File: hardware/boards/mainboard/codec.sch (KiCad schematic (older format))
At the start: 22 parts, among them U1 CS42448

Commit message: mainboard
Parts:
- removed C11, C12, C13, C14: 4.7uf, Mainboard:AVX-A, symbol Mainboard-eagle-import:TANTALUM-SMD-4.7UF-16V(AVX-A)
- added C11, C12, C13, C14: 4.7uF, Capacitors_Tantalum_SMD:CP_Tantalum_Case-A_EIA-3216-18_Reflow, symbol Device:CP
- R1, R2, R3: footprint Mainboard:R0805 -> Resistors_SMD:R_0805
- R4: footprint Mainboard:R0805 -> Oddities:NetTie-I_Connected_SMD; symbol Mainboard-eagle-import:ZERO-OHM-LINK -> Device:Net-Tie_2
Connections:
- net 3V3: no longer C15.2, R2.1, R3.1, U1.3 (~RST~)
- net AGND: now also C11.2, C12.2, C13.2, C14.2
- net GND: no longer C15.1, R4.1, U1.2 (AD1/CDIN), U1.23 (DGND@23), U1.62 (DGND@62), U1.7 (DGND@7)
- net at U1.45 (AIN1-): now also C11.1
- net at U1.47 (AIN2-): now also C12.1
- net at U1.49 (AIN3-): now also C13.1
- net at U1.51 (AIN4-): now also C14.1
- new net: R4.1, U1.23 (DGND@23), U1.62 (DGND@62), U1.7 (DGND@7)
- new net +3V3: C15.2, R2.1, R3.1, U1.3 (~RST~)
- no-connect marks 0 -> 16
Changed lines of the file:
@@
 $Descr User 13529 9224
 encoding utf-8
-Sheet 5 13
+Sheet 5 12
 Title ""
 Date ""
@@
 Wire Wire Line
 	4600 6500 4900 6500
-Text GLabel 4600 6700 0    10   BiDi ~ 0
-GND
 Wire Wire Line
 	4900 5400 4900 5500
@@
 Wire Wire Line
 	6300 7300 6300 8350
-Wire Wire Line
-	6300 8350 6650 8350
 Connection ~ 6100 7300
 Connection ~ 6200 7300
 Connection ~ 6300 7300
-Text GLabel 6100 7300 0    10   BiDi ~ 0
-GND
 Wire Wire Line
 	4150 650  4150 450
-Text GLabel 4150 650  0    10   BiDi ~ 0
-GND
 Wire Wire Line
 	7100 2100 7100 2200
@@
 	4300 7000 4900 7000
 Connection ~ 4100 7000
-Text GLabel 4200 7000 2    70   BiDi ~ 0
-3V3
 Connection ~ 4300 7000
 Wire Wire Line
 	3550 150  4150 150
-Wire Wire Line
-	4150 150  4750 150
-Connection ~ 4150 150
 Text GLabel 3550 150  0    70   BiDi ~ 0
-3V3
++3V3
 Wire Wire Line
 	1150 2500 4900 2500
@@
 	4900 2700 4800 2700
 Wire Wire Line
-	3050 2000 4600 2000
-Wire Wire Line
-	4600 2000 4600 3300
+	4600 2150 4600 3300
 Wire Wire Line
 	4600 3300 4900 3300
@@
 Wire Wire Line
 	4650 3900 4900 3900
-Wire Wire Line
-	9750 1850 10200 1850
-Text Label 10200 1850 0    70   ~ 0
+Text Label 12200 1100 0    70   ~ 0
 AGND
 Wire Wire Line
@@
 Wire Wire Line
 	7350 8350 7350 7500
-Wire Wire Line
-	6950 8350 7350 8350
 Connection ~ 6700 7300
 Connection ~ 9100 7500
@@
 $EndComp
 $Comp
-L Mainboard-eagle-import:3.3V #SUPPLY?
-U 1 1 9BB82FD5
-P 3200 6900
-AR Path="/9BB82FD5" Ref="#SUPPLY?"  Part="1"
-AR Path="/5D773153/9BB82FD5" Ref="#SUPPLY01"  Part="1"
-F 0 "#SUPPLY01" H 3200 6900 50  0001 C CNN
-F 1 "3.3V" H 3200 7010 59  0000 C BNN
-F 2 "" H 3200 6900 50  0001 C CNN
-F 3 "" H 3200 6900 50  0001 C CNN
-	1    3200 6900
-	1    0    0    -1
-$EndComp
-$Comp
 L Mainboard-eagle-import:GND #GND?
 U 1 1 78C00C8D
@@
 AR Path="/5D773153/1D06DB6F" Ref="R2"  Part="1"
 F 0 "R2" H 3950 6800 59  0000 L BNN
-F 1 "2K" H 3950 6620 59  0001 L BNN
-F 2 "Mainboard:R0805" H 4100 6750 50  0001 C CNN
+F 1 "2K" H 3950 6620 59  0000 L BNN
+F 2 "Resistors_SMD:R_0805" H 4100 6750 50  0001 C CNN
 F 3 "" H 4100 6750 50  0001 C CNN
 	1    4100 6750
@@
 AR Path="/5D773153/21D49CC9" Ref="R3"  Part="1"
 F 0 "R3" H 4150 6650 59  0000 L BNN
-F 1 "2K" H 4150 6470 59  0001 L BNN
-F 2 "Mainboard:R0805" H 4300 6600 50  0001 C CNN
+F 1 "2K" H 4150 6470 59  0000 L BNN
+F 2 "Resistors_SMD:R_0805" H 4300 6600 50  0001 C CNN
 F 3 "" H 4300 6600 50  0001 C CNN
 	1    4300 6600
@@
 $EndComp
 $Comp
-L Mainboard-eagle-import:TANTALUM-SMD-4.7UF-16V(AVX-A) C?
-U 1 1 193FF8E5
-P 1150 2650
-AR Path="/193FF8E5" Ref="C?"  Part="1"
-AR Path="/5D773153/193FF8E5" Ref="C11"  Part="1"
-F 0 "C11" H 900 2800 42  0000 L BNN
-F 1 "4.7uf" H 1200 2800 42  0000 L BNN
-F 2 "Mainboard:AVX-A" H 1150 2650 50  0001 C CNN
-F 3 "" H 1150 2650 50  0001 C CNN
-	1    1150 2650
-	0    1    1    0
-$EndComp
-$Comp
-L Mainboard-eagle-import:TANTALUM-SMD-4.7UF-16V(AVX-A) C?
-U 1 1 0925562E
-P 1500 2950
-AR Path="/0925562E" Ref="C?"  Part="1"
-AR Path="/5D773153/0925562E" Ref="C12"  Part="1"
-F 0 "C12" H 1250 3100 42  0000 L BNN
-F 1 "4.7uf" H 1550 3100 42  0000 L BNN
-F 2 "Mainboard:AVX-A" H 1500 2950 50  0001 C CNN
-F 3 "" H 1500 2950 50  0001 C CNN
-	1    1500 2950
-	0    1    1    0
-$EndComp
-$Comp
-L Mainboard-eagle-import:TANTALUM-SMD-4.7UF-16V(AVX-A) C?
-U 1 1 EF1AB486
-P 2250 3550
-AR Path="/EF1AB486" Ref="C?"  Part="1"
-AR Path="/5D773153/EF1AB486" Ref="C14"  Part="1"
-F 0 "C14" H 2000 3700 42  0000 L BNN
-F 1 "4.7uf" H 2300 3700 42  0000 L BNN
-F 2 "Mainboard:AVX-A" H 2250 3550 50  0001 C CNN
-F 3 "" H 2250 3550 50  0001 C CNN
-	1    2250 3550
-	0    1    1    0
-$EndComp
-$Comp
-L Mainboard-eagle-import:TANTALUM-SMD-4.7UF-16V(AVX-A) C?
-U 1 1 711B141C
-P 1900 3250
-AR Path="/711B141C" Ref="C?"  Part="1"
-AR Path="/5D773153/711B141C" Ref="C13"  Part="1"
-F 0 "C13" H 1650 3400 42  0000 L BNN
-F 1 "4.7uf" H 1950 3400 42  0000 L BNN
-F 2 "Mainboard:AVX-A" H 1900 3250 50  0001 C CNN
-F 3 "" H 1900 3250 50  0001 C CNN
-	1    1900 3250
-	0    1    1    0
-$EndComp
-$Comp
 L Mainboard-eagle-import:R-US_R0805 R?
 U 1 1 00F92E51
@@
 AR Path="/5D773153/00F92E51" Ref="R1"  Part="1"
 F 0 "R1" H 1950 7900 59  0000 L BNN
-F 1 "2K" H 1950 7720 59  0001 L BNN
-F 2 "Mainboard:R0805" H 2100 7850 50  0001 C CNN
+F 1 "2K" H 1950 7720 59  0000 L BNN
+F 2 "Resistors_SMD:R_0805" H 2100 7850 50  0001 C CNN
 F 3 "" H 2100 7850 50  0001 C CNN
 	1    2100 7850
@@
 $EndComp
 $Comp
-L Mainboard-eagle-import:ZERO-OHM-LINK R?
+L Device:Net-Tie_2 R?
 U 1 1 64BB04EC
 P 6800 8350
@@
 F 0 "R4" H 6650 8400 42  0000 L BNN
 F 1 "0" H 6650 8250 42  0000 L BNN
-F 2 "Mainboard:R0805" H 6800 8350 50  0001 C CNN
+F 2 "Oddities:NetTie-I_Connected_SMD" H 6800 8350 50  0001 C CNN
 F 3 "" H 6800 8350 50  0001 C CNN
 	1    6800 8350
@@
 Wire Wire Line
 	9000 1200 9650 1200
-Wire Wire Line
-	11250 1100 11500 1100
-Wire Wire Line
-	11500 1100 11500 1700
-Wire Wire Line
-	11500 1700 9750 1700
-Wire Wire Line
-	9750 1700 9750 1850
 $Sheet
 S 1000 1000 1100 700
@@
 F4 "AGND" O L 1000 1250 50
 $EndSheet
-Wire Wire Line
-	4900 1150 4900 2400
 Wire Wire Line
 	2100 1150 4900 1150
@@
 	2850 1900 4700 1900
 Wire Wire Line
-	3050 2000 3050 2150
-Wire Wire Line
-	3050 2150 2850 2150
-Wire Wire Line
 	4650 3900 4650 4200
 Wire Wire Line
@@
 Wire Wire Line
 	1950 4050 2550 4050
+Wire Wire Line
+	2850 2150 4600 2150
+Wire Wire Line
+	11250 1100 12200 1100
+Wire Wire Line
+	4900 2400 4900 1150
+Wire Wire Line
+	6300 8350 6700 8350
+Wire Wire Line
+	6900 8350 7350 8350
+$Comp
+L Device:CP C11
+U 1 1 5D92D0F0
+P 1150 2650
+F 0 "C11" H 1268 2696 50  0000 L CNN
+F 1 "4.7uF" H 1268 2605 50  0000 L CNN
+F 2 "Capacitors_Tantalum_SMD:CP_Tantalum_Case-A_EIA-3216-18_Reflow" H 1188 2500 50  0001 C CNN
+F 3 "~" H 1150 2650 50  0001 C CNN
+	1    1150 2650
+	1    0    0    -1
+$EndComp
+$Comp
+L Device:CP C12
+U 1 1 5D92DE00
+P 1500 2950
+F 0 "C12" H 1618 2996 50  0000 L CNN
+F 1 "4.7uF" H 1618 2905 50  0000 L CNN
+F 2 "Capacitors_Tantalum_SMD:CP_Tantalum_Case-A_EIA-3216-18_Reflow" H 1538 2800 50  0001 C CNN
+F 3 "~" H 1500 2950 50  0001 C CNN
+	1    1500 2950
+	1    0    0    -1
+$EndComp
+$Comp
+L Device:CP C13
+U 1 1 5D92E6E2
+P 1900 3250
+F 0 "C13" H 2018 3296 50  0000 L CNN
+F 1 "4.7uF" H 2018 3205 50  0000 L CNN
+F 2 "Capacitors_Tantalum_SMD:CP_Tantalum_Case-A_EIA-3216-18_Reflow" H 1938 3100 50  0001 C CNN
+F 3 "~" H 1900 3250 50  0001 C CNN
+	1    1900 3250
+	1    0    0    -1
+$EndComp
+$Comp
+L Device:CP C14
+U 1 1 5D92F56D
+P 2250 3550
+F 0 "C14" H 2368 3596 50  0000 L CNN
+F 1 "4.7uF" H 2368 3505 50  0000 L CNN
+F 2 "Capacitors_Tantalum_SMD:CP_Tantalum_Case-A_EIA-3216-18_Reflow" H 2288 3400 50  0001 C CNN
+F 3 "~" H 2250 3550 50  0001 C CNN
+	1    2250 3550
+	1    0    0    -1
+$EndComp
+Text GLabel 3200 6900 0    70   BiDi ~ 0
++3V3
+NoConn ~ 4900 4900
+NoConn ~ 4900 4800
+NoConn ~ 4900 4600
+NoConn ~ 4900 4500
+NoConn ~ 4900 4000
+NoConn ~ 4900 3700
+NoConn ~ 4900 6800
+NoConn ~ 7900 2500
+NoConn ~ 7900 2800
+NoConn ~ 7900 3100
+NoConn ~ 7900 3400
+NoConn ~ 7900 3700
+NoConn ~ 7900 4000
+NoConn ~ 7900 4300
+NoConn ~ 7900 4600
+NoConn ~ 7900 6200
 $EndSCHEMATC

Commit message: mainboard refactor
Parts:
- R4: footprint Oddities:NetTie-I_Connected_SMD -> Mainboard:NetTie-I_Connected_SMD_small
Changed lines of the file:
@@
 F 0 "R4" H 6650 8400 42  0000 L BNN
 F 1 "0" H 6650 8250 42  0000 L BNN
-F 2 "Oddities:NetTie-I_Connected_SMD" H 6800 8350 50  0001 C CNN
+F 2 "Mainboard:NetTie-I_Connected_SMD_small" H 6800 8350 50  0001 C CNN
 F 3 "" H 6800 8350 50  0001 C CNN
 	1    6800 8350

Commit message: mainboard v1.6
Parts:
- C22: footprint Capacitors_SMD:C_0805_HandSoldering -> Capacitor_SMD:C_1206_3216Metric
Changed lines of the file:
@@
 F 0 "C22" H 8550 7250 42  0000 L BNN
 F 1 "100uf" H 8550 7100 42  0000 L BNN
-F 2 "Capacitors_SMD:C_0805_HandSoldering" H 8700 7200 50  0001 C CNN
+F 2 "Capacitor_SMD:C_1206_3216Metric" H 8700 7200 50  0001 C CNN
 F 3 "" H 8700 7200 50  0001 C CNN
 	1    8700 7200

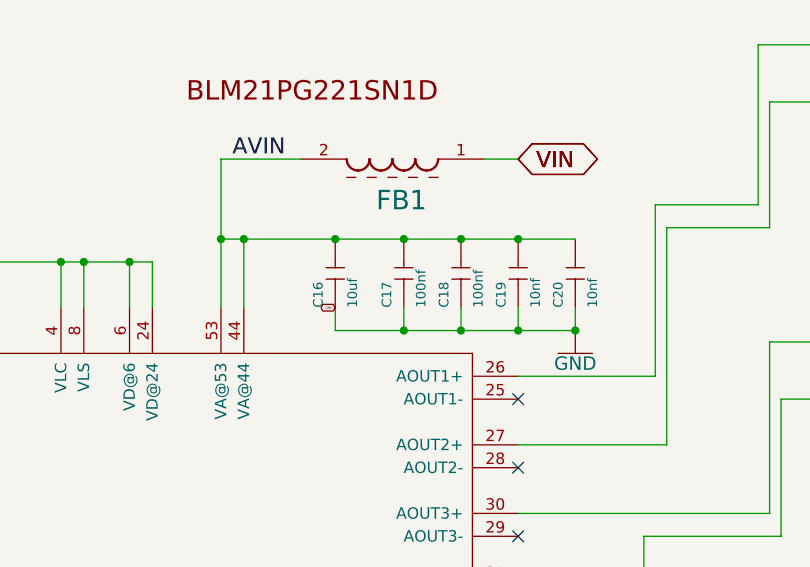
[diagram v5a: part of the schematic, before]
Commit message: silkscreen impr. & changed 100nF to 0.1uF
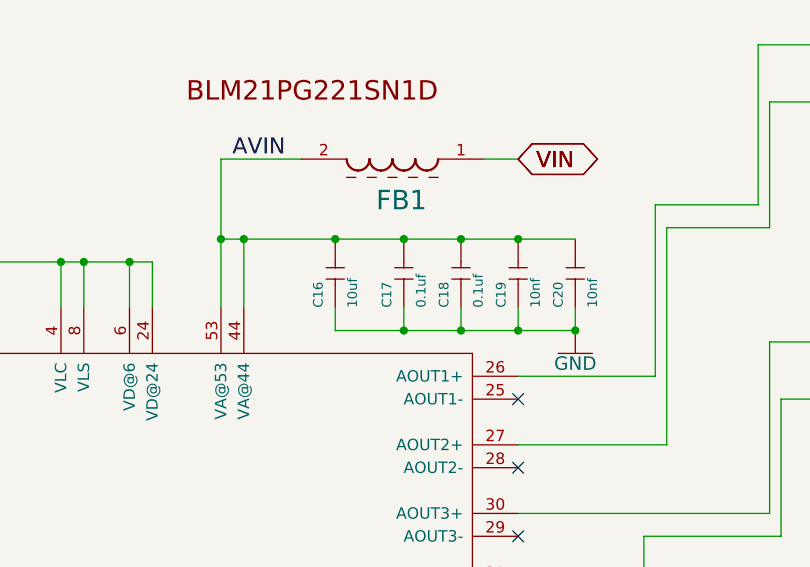
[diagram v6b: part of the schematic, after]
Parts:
- C17, C18: value 100nf -> 0.1uf
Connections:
- net GND: no longer names the net of C16.1, C17.1, C18.1, C19.1, C20.1
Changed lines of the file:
@@
 Connection ~ 7650 2200
 Connection ~ 7400 2200
-Text GLabel 7100 2100 0    10   BiDi ~ 0
-GND
 Wire Wire Line
 	4900 6300 4100 6300
@@
 AR Path="/5D773153/1203FA24" Ref="C17"  Part="1"
 F 0 "C17" H 7250 2000 42  0000 L BNN
-F 1 "100nf" H 7250 1850 42  0000 L BNN
+F 1 "0.1uf" H 7250 1850 42  0000 L BNN
 F 2 "Capacitors_SMD:C_0805_HandSoldering" H 7400 1950 50  0001 C CNN
 F 3 "" H 7400 1950 50  0001 C CNN
@@
 AR Path="/5D773153/14EE9965" Ref="C18"  Part="1"
 F 0 "C18" H 7500 2000 42  0000 L BNN
-F 1 "100nf" H 7500 1850 42  0000 L BNN
+F 1 "0.1uf" H 7500 1850 42  0000 L BNN
 F 2 "Capacitors_SMD:C_0805_HandSoldering" H 7650 1950 50  0001 C CNN
 F 3 "" H 7650 1950 50  0001 C CNN
